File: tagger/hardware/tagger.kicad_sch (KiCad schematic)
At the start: 39 parts, among them J1 SD_CARD, J4 SWD, J7 TETHER_DATA, J8 DISPLAY, J9 IO_CONN, SW24 BOOT0, SW26 NRST, U1 LSM6DS3, U3 STM32F401RETx, U8 MAX98357A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

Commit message: chore(tagger): schematic reorganization
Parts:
- removed LS2: Speaker, symbol Device:Speaker
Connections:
- net BTN_RELOAD+ is gone; now on net GND: J9.22 (Pin_22)
- net BTN_TRIGGER+ is gone; now on net GND: J9.20 (Pin_20)
- net MOTOR+ is gone; now on net GND: J9.6 (Pin_6)
- net SWD_SWO: now also U3.55 (PB3)
- net BTN_RELOAD- renamed BTN_RELOAD
- net BTN_TRIGGER- renamed BTN_TRIGGER
- net CAP_DOUT renamed GRIP_DOUT
- net FRONT_G_IR renamed FRONT_IR
- net FRONT_R_7.4v renamed VDD
- net FRONT_Y_LED? renamed FRONT_LED?
- net MOTOR- renamed MOTOR
- no-connect marks 3 -> 4
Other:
- note added: "Front Connector: Black - GND Red - VDD (7.4-8.4v) White - 3.3v Green - IR Sensor Yellow - LED Data"
- note added: "SD Card"
- note added: "TODO: select better crystal 8mhz"
- note removed: "TODO: select better crystal 84mhz"
- moved on the sheet: C100, C101, C102, C103, C2, C61, C62, C66, C68, C7, C8, C99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

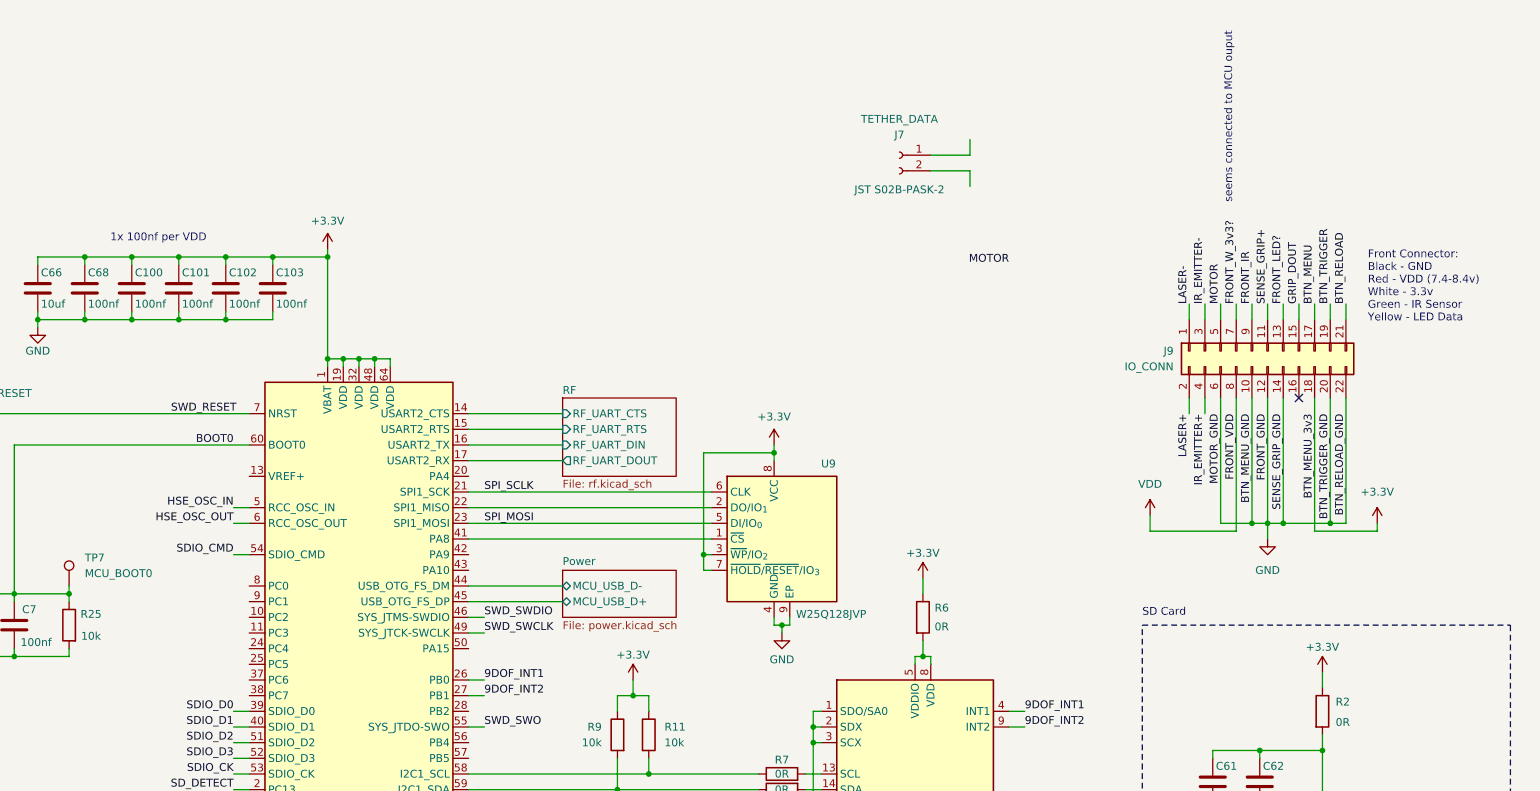
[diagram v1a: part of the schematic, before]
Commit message: feat(tagger): add notes to schematic
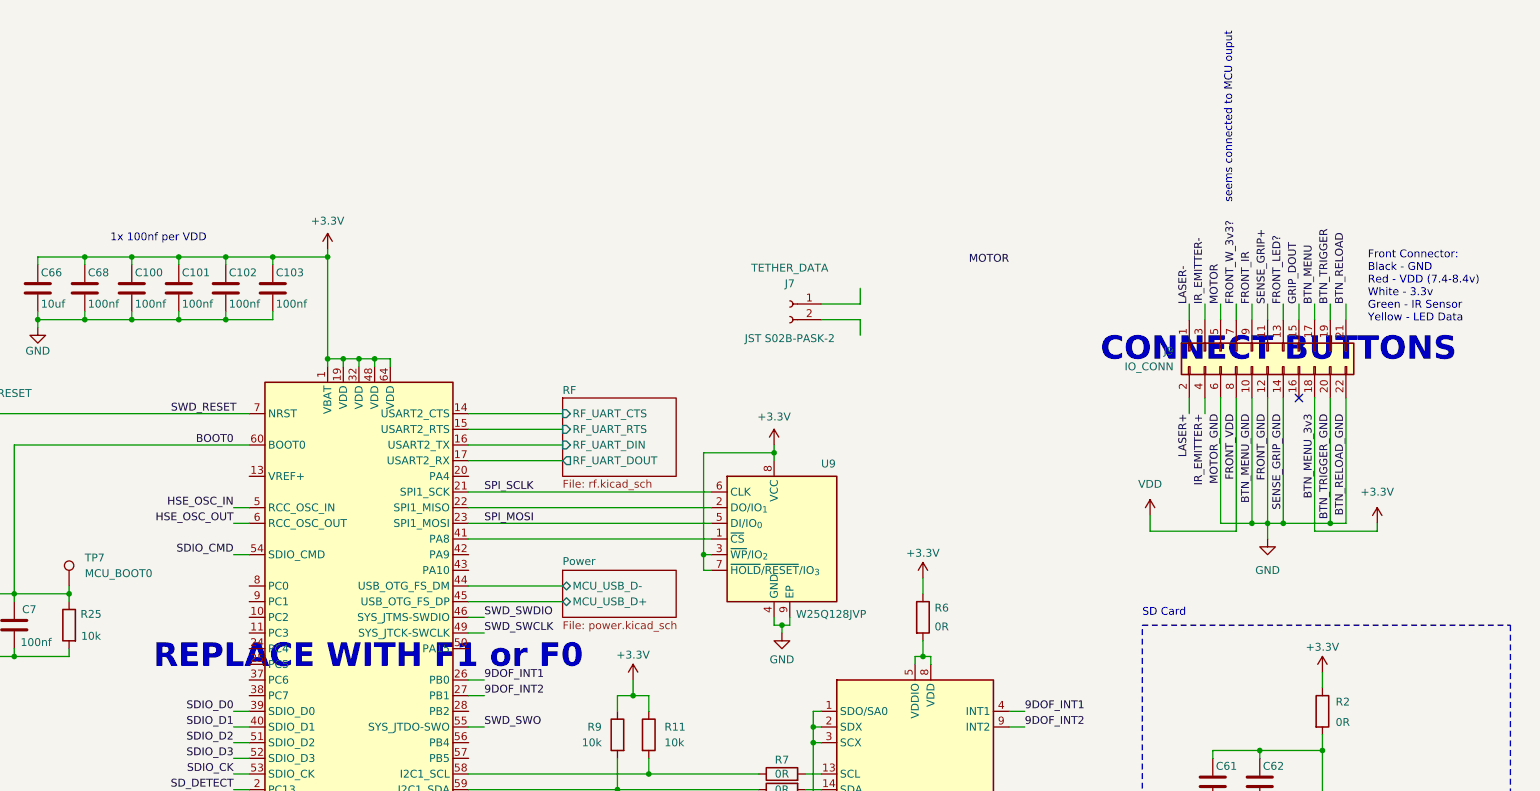
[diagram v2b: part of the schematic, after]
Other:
- note added: "CONNECT BUTTONS"
- note added: "REPLACE WITH F1 or F0"
- moved on the sheet: J7
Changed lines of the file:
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@@
 		)
 	)
+	(text "CONNECT BUTTONS"
+		(exclude_from_sim no)
+		(at 245.618 36.576 0)
+		(effects
+			(font
+				(size 3.81 3.81)
+				(thickness 0.762)
+				(bold yes)
+				(color 255 0 0 1)
+			)
+		)
+	)
 	(text "ST7789V2"
 		(exclude_from_sim no)
@@
 		)
 	)
+	(text "REPLACE WITH F1 or F0"
+		(exclude_from_sim no)
+		(at 98.044 86.36 0)
+		(effects
+			(font
+				(size 3.81 3.81)
+				(thickness 0.762)
+				(bold yes)
+				(color 255 0 0 1)
+			)
+		)
+	)
 	(text "TODO: select better crystal 8mhz\n"
 		(exclude_from_sim no)
@@
 	(wire
 		(pts
-			(xy 195.58 2.54) (xy 195.58 5.08)
+			(xy 177.8 26.67) (xy 177.8 29.21)
 		)
 		(stroke
@@
 	(wire
 		(pts
-			(xy 189.23 7.62) (xy 195.58 7.62)
+			(xy 171.45 31.75) (xy 177.8 31.75)
 		)
 		(stroke
@@
 	(wire
 		(pts
-			(xy 189.23 5.08) (xy 195.58 5.08)
+			(xy 171.45 29.21) (xy 177.8 29.21)
 		)
 		(stroke
@@
 	(wire
 		(pts
-			(xy 195.58 7.62) (xy 195.58 10.16)
+			(xy 177.8 31.75) (xy 177.8 34.29)
 		)
 		(stroke
@@
 	(symbol
 		(lib_id "Connector:Conn_01x02_Socket")
-		(at 184.15 5.08 0)
+		(at 166.37 29.21 0)
 		(mirror y)
 		(unit 1)
@@
 		(dnp no)
 		(property "Reference" "J7"
-			(at 184.15 1.778 0)
+			(at 166.37 25.908 0)
 			(effects
 				(font
@@
 		)
 		(property "Value" "TETHER_DATA"
-			(at 184.15 -0.762 0)
+			(at 166.37 23.368 0)
 			(effects
 				(font
@@
 		)
 		(property "Footprint" ""
-			(at 184.15 5.08 0)
+			(at 166.37 29.21 0)
 			(effects
 				(font
@@
 		)
 		(property "Datasheet" "~"
-			(at 184.15 5.08 0)
+			(at 166.37 29.21 0)
 			(effects
 				(font
@@
 		)
 		(property "Description" "Generic connector, single row, 01x02, script generated"
-			(at 184.15 5.08 0)
+			(at 166.37 29.21 0)
 			(effects
 				(font
@@
 		)
 		(property "Conn" "JST S02B-PASK-2"
-			(at 184.15 10.668 0)
+			(at 166.37 34.798 0)
 			(effects
 				(font

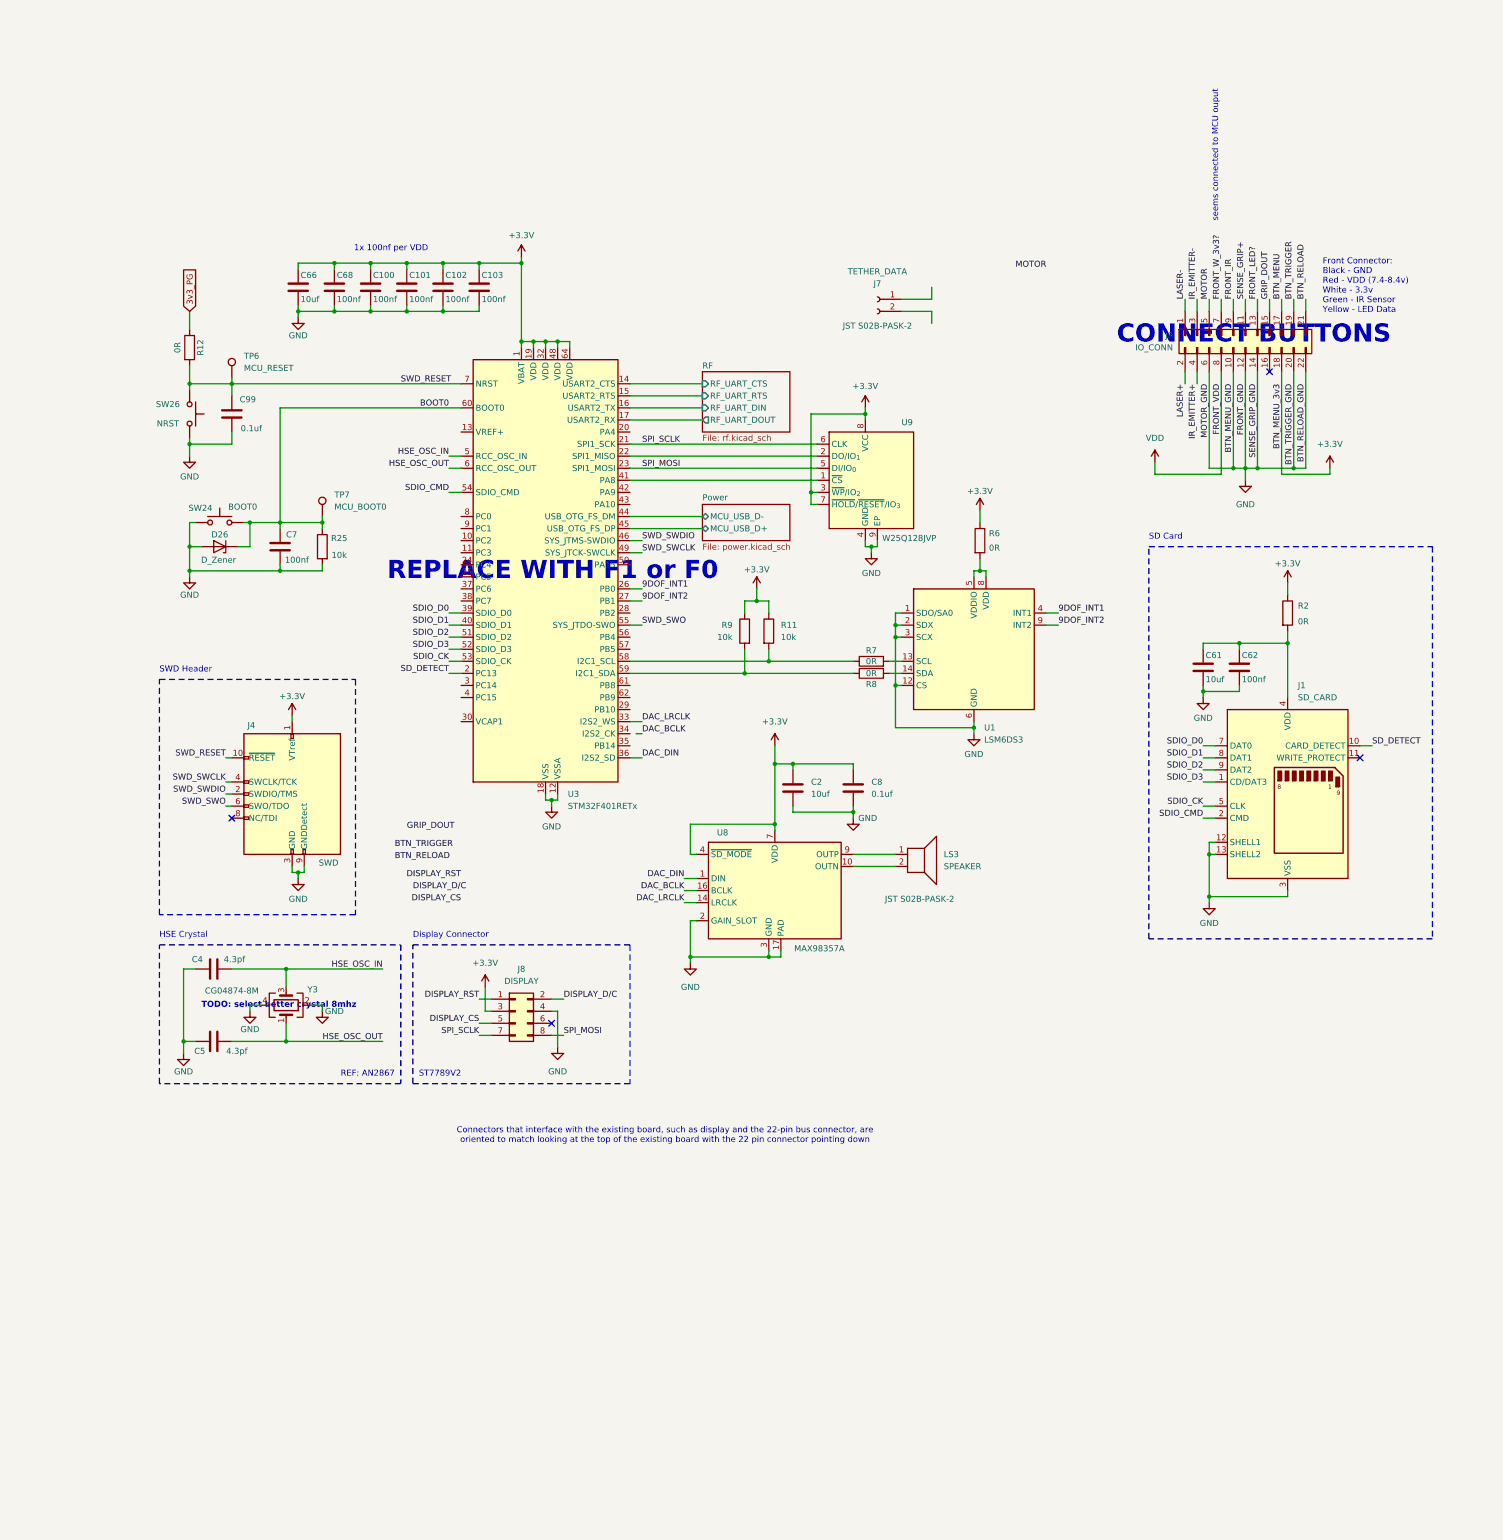
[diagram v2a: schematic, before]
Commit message: feat: schematic organization
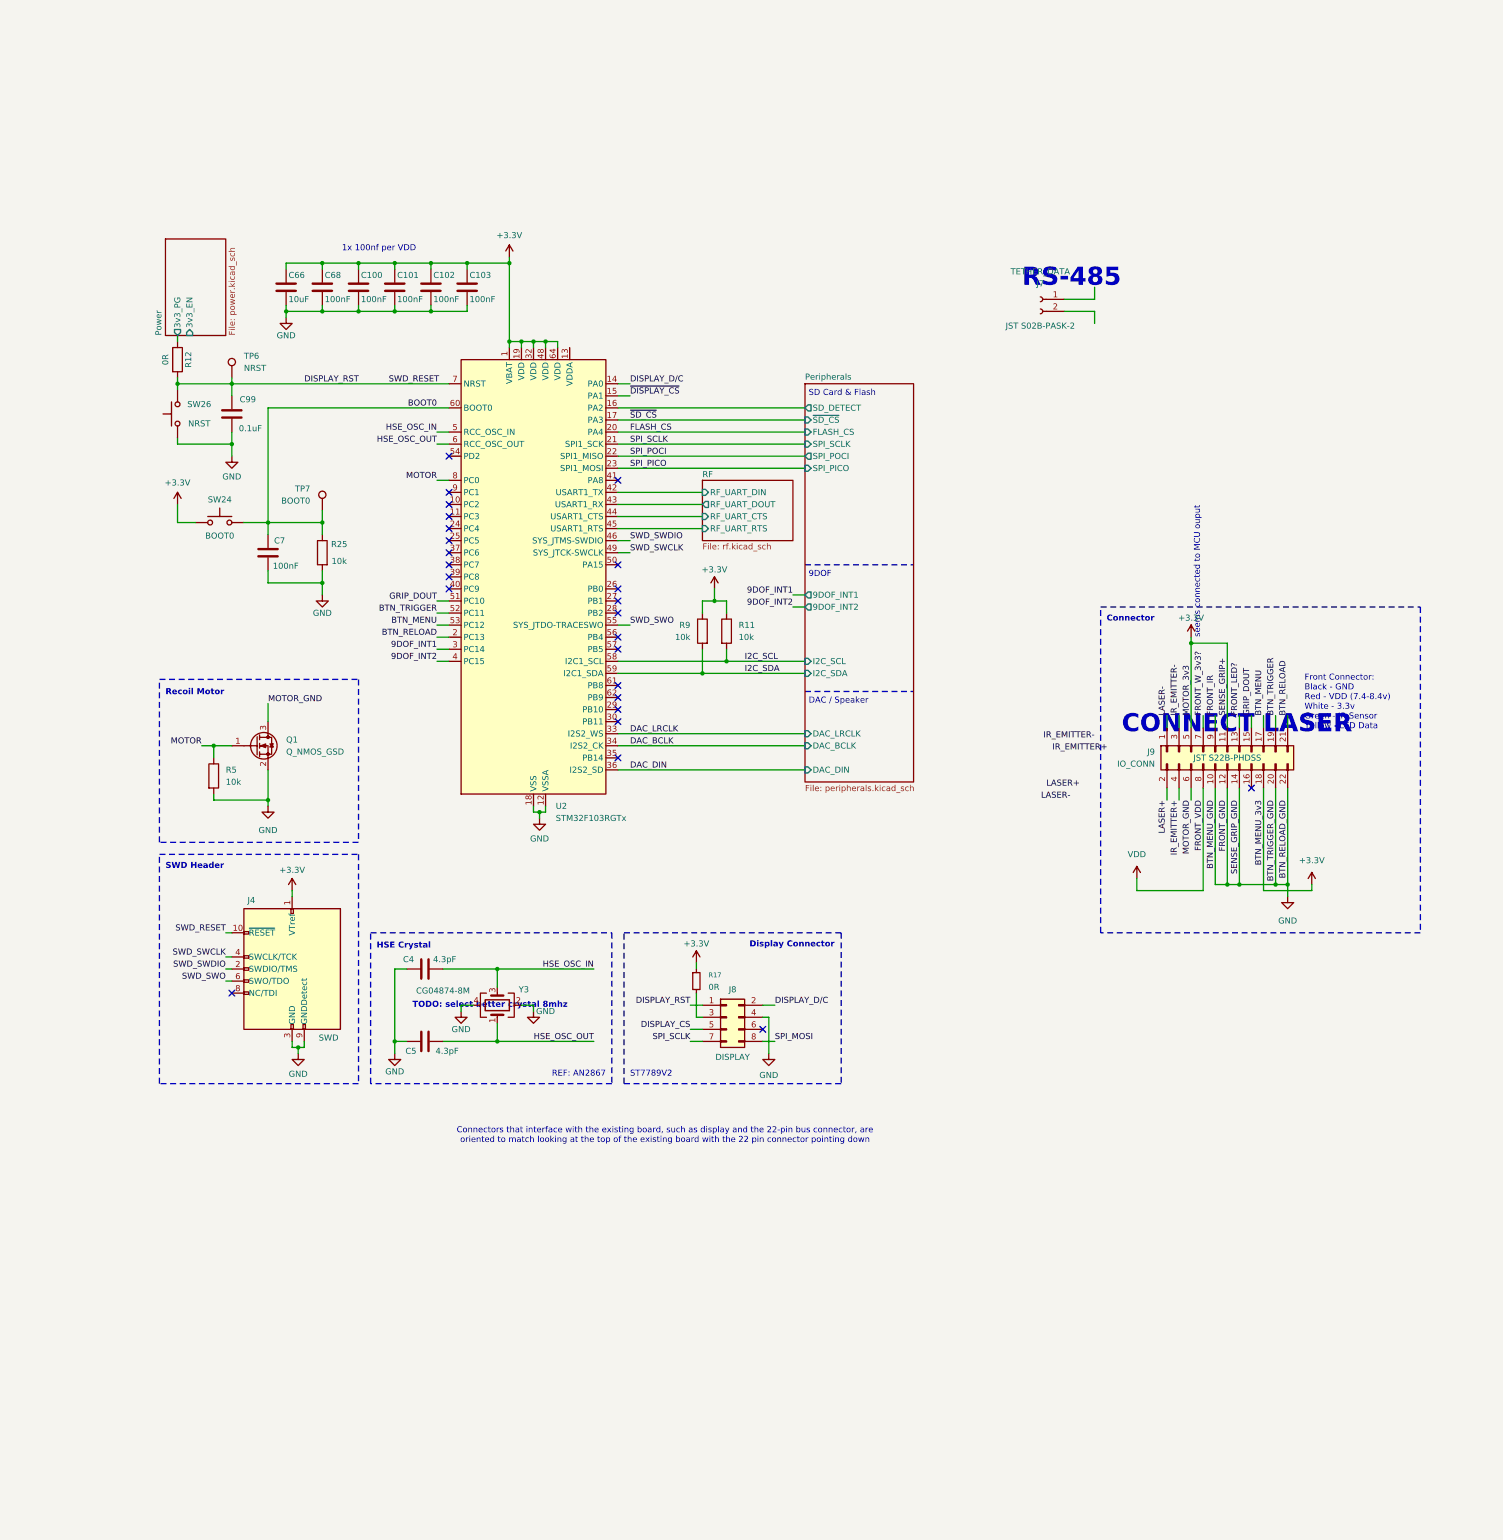
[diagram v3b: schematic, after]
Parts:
- removed C2, C61: 10uf, symbol Device:C
- removed C62: 100nf, symbol Device:C
- removed C8: 0.1uf, symbol Device:C
- removed D26: D_Zener, symbol Device:D_Zener
- removed J1: SD_CARD, symbol Connector:SD_Card_Receptacle
- removed LS3: SPEAKER, symbol Device:Speaker
- removed R2, R6, R7, R8: 0R, symbol Device:R
- removed U1: LSM6DS3, Package_LGA:LGA-14_3x2.5mm_P0.5mm_LayoutBorder3x4y, symbol Sensor_Motion:LSM6DS3
- removed U3: STM32F401RETx, Package_QFP:LQFP-64_10x10mm_P0.5mm, symbol MCU_ST_STM32F4:STM32F401RETx
- removed U8: MAX98357A, Package_DFN_QFN:TQFN-16-1EP_3x3mm_P0.5mm_EP1.23x1.23mm, symbol Audio:MAX98357A
- removed U9: W25Q128JVP, Package_SON:WSON-8-1EP_6x5mm_P1.27mm_EP3.4x4.3mm, symbol Memory_Flash:W25Q128JVP
- added Q1: Q_NMOS_GSD, symbol Transistor_FET:Q_NMOS_GSD
- added R17: 0R, Resistor_SMD:R_0201_0603Metric_Pad0.64x0.40mm_HandSolder, symbol Device:R_Small
- added R5: 10k, Resistor_SMD:R_0201_0603Metric_Pad0.64x0.40mm_HandSolder, symbol Device:R
- added U2: STM32F103RGTx, Package_QFP:LQFP-64_10x10mm_P0.5mm, symbol MCU_ST_STM32F1:STM32F103RGTx
- C100, C101, C102, C103, C68, C7: value 100nf -> 100nF; footprint (none) -> Capacitor_SMD:C_0201_0603Metric_Pad0.64x0.40mm_HandSolder
- C4, C5: value 4.3pf -> 4.3pF; footprint (none) -> Capacitor_SMD:C_0201_0603Metric_Pad0.64x0.40mm_HandSolder
- C66: value 10uf -> 10uF; footprint (none) -> Capacitor_SMD:C_0201_0603Metric_Pad0.64x0.40mm_HandSolder
- C99: value 0.1uf -> 0.1uF; footprint (none) -> Capacitor_SMD:C_0201_0603Metric_Pad0.64x0.40mm_HandSolder
- J7: footprint (none) -> Connector_PinHeader_2.00mm:PinHeader_1x02_P2.00mm_Horizontal
- J8: footprint (none) -> Connector_PinHeader_2.00mm:PinHeader_2x04_P2.00mm_Vertical
- J9: footprint (none) -> Connector_PinSocket_2.00mm:PinSocket_2x11_P2.00mm_Horizontal; Conn (none) -> JST S22B-PHDSS
- R11, R12, R25, R9: footprint (none) -> Resistor_SMD:R_0201_0603Metric_Pad0.64x0.40mm_HandSolder
- SW24, SW26: footprint (none) -> Button_Switch_SMD:SW_Push_1P1T_NO_CK_KMR2
- TP6: value MCU_RESET -> NRST; footprint (none) -> TestPoint:TestPoint_Pad_D2.5mm
- TP7: value MCU_BOOT0 -> BOOT0; footprint (none) -> TestPoint:TestPoint_Pad_D2.5mm
- Y3: footprint (none) -> Crystal:Crystal_SMD_0603-4Pin_6.0x3.5mm
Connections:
- net SENSE_GRIP+ is gone; now on net +3.3V: J9.11 (Pin_11)
- net SWD_RESET is gone; now on net DISPLAY_RST: C99.2, J4.10 (~{RESET}), R12.2, SW26.2, TP6.1
- net +3.3V: now also J9.5 (Pin_5), SW24.1, R17.1, U2.1 (VBAT), U2.19 (VDD), U2.32 (VDD), U2.48 (VDD), U2.64 (VDD); no longer J8.3 (Pin_3)
- net 9DOF_INT1: now also U2.3 (PC14)
- net 9DOF_INT2: now also U2.4 (PC15)
- net BOOT0: now also U2.60 (BOOT0)
- net BTN_MENU: now also U2.53 (PC12)
- net BTN_RELOAD: now also U2.2 (PC13)
- net BTN_TRIGGER: now also U2.52 (PC11)
- net DAC_BCLK: now also U2.34 (PB13)
- net DAC_DIN: now also U2.36 (PB15)
- net DAC_LRCLK: now also U2.33 (PB12)
- net DISPLAY_D/C: now also U2.14 (PA0)
- net DISPLAY_RST: now also U2.7 (NRST)
- net GND: now also Q1.2 (S), R5.2, U2.12 (VSSA), U2.18 (VSS), U2.31 (VSS), U2.47 (VSS), U2.63 (VSS); no longer J9.6 (Pin_6), SW24.1
- net GRIP_DOUT: now also U2.51 (PC10)
- net HSE_OSC_IN: now also U2.5 (PD0)
- net HSE_OSC_OUT: now also U2.6 (PD1)
- net MOTOR: now also Q1.1 (G), R5.1, U2.8 (PC0); no longer J9.5 (Pin_5)
- net RF/RF_UART_CTS: now also U2.44 (PA11)
- net RF/RF_UART_DIN: now also U2.42 (PA9)
- net RF/RF_UART_DOUT: now also U2.43 (PA10)
- net RF/RF_UART_RTS: now also U2.45 (PA12)
- net SPI_SCLK: now also U2.21 (PA5)
- net SWD_SWCLK: now also U2.49 (PA14)
- net SWD_SWDIO: now also U2.46 (PA13)
- net SWD_SWO: now also U2.55 (PB3)
- net I2C_SDA: now reaches R9.2
- net I2C_SDA: now also U2.59 (PB7)
- net I2C_SCL: now reaches R11.2
- net I2C_SCL: now also U2.58 (PB6)
- net 3v3_PG renamed Power/3v3_PG
- new net: J8.3 (Pin_3), R17.2
- new net FLASH_CS: U2.20 (PA4)
- new net MOTOR_GND: J9.6 (Pin_6), Q1.3 (D)
- new net Peripherals/SD_DETECT: U2.16 (PA2)
- new net SPI_PICO: U2.23 (PA7)
- new net SPI_POCI: U2.22 (PA6)
- new net ~{DISPLAY_CS}: U2.15 (PA1)
- new net ~{SD_CS}: U2.17 (PA3)
- no-connect marks 4 -> 25
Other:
- added sheet Peripherals (peripherals.kicad_sch)
- sheet Power ports: added 3v3_EN, 3v3_PG; removed MCU_USB_D+, MCU_USB_D-
- note added: "9DOF"
- note added: "CONNECT LASER"
- note added: "Connector"
- note added: "DAC / Speaker"
- note added: "RS-485"
- note added: "Recoil Motor"
- note added: "SD Card & Flash"
- note removed: "CONNECT BUTTONS"
- note removed: "REPLACE WITH F1 or F0"
- note removed: "SD Card"
- moved on the sheet: C100, C101, C102, C103, C4, C5, C66, C68, C7, J4, J7, J8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
